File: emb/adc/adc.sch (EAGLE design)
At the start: 21 parts, among them IC1 AD623N, IC2 MCP3008, Q1 RD06HVF1, Q2 RD06HVF1, Q3 RD06HVF1, Q4 RD06HVF1

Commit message: new board
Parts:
- removed LED_YELLOW: (no value), adafruit:LED5MM
- removed Q4: RD06HVF1, transistor-power:RD06HVF1
- added R10, R9: 12K, rcl:R-US_0207/10
- IC1: value AD623N -> LM358N; device analog-devices:AD623N -> linear:LM358N
- Q1, Q2, Q3: value RD06HVF1 -> (none); device transistor-power:RD06HVF1 -> adafruit:MOSFET-NGDS_TO220V
- R1: value (none) -> 100K
- R2: value (none) -> 7.5K
- R3: value (none) -> 1.2K
- R4: value (none) -> 3.3K
- R5: value (none) -> 200
- R6, R7: value (none) -> 160
- R8: value (none) -> 12K
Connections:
- net N$12 renamed 3.3V
- removed net L_Y: J1.4, Q4.G
- removed net N$14: LED_RED.A, Q1.D
- removed net N$16: LED_GREEN.C, R6.1
- removed net N$17: LED_GREEN.A, Q2.D
- removed net N$18: LED_BLUE.C, R7.1
- removed net N$19: LED_YELLOW.C, R8.1
- removed net N$20: LED_BLUE.A, Q3.D
- removed net N$21: LED_YELLOW.A, Q4.D
- removed net VCC: IC2.GND
- new net 4.5V: IC1P.V+, R2.2, R3.2
- new net N$12: LED_GREEN.A, R6.1
- new net N$8: LED_BLUE.A, R7.1
- net 0V: now also D1.A, IC1A.-IN, IC1P.V-, IC2.GND, R10.1, R4.2, R8.2, R9.2; no longer IC1.-, IC1.REF, Q4.S, R3.2
- net 12V: now also R2.1; no longer D1.A, IC1.+V, R4.2, R8.2
- net L_B: now also R10.2
- net L_G: now also R9.1
- net L_R: now also R8.1
- net N$1: now also D1.C, IC1A.+IN; no longer IC1.RG@1
- net N$13: now also LED_GREEN.C, Q2.D; no longer LED_RED.C, R5.1
- net N$2: now also LED_BLUE.C, Q3.D; no longer IC1.RG@2, R1.1
- net N$3: now also LED_RED.A, R5.1; no longer D1.C, R2.1
- net N$6: now also LED_RED.C, Q1.D; no longer IC1.+, R2.2
- net N$7: now also IC1A.OUT, R1.1; no longer IC1.OUT
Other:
- note added: "1.9 - rød"
- note added: "3.2 - grøn og blå"
- note added: "forward voltage"
- note removed: "5V"
- moved on the sheet: D1, LED_BLUE, LED_GREEN, LED_RED, R1, R2, R3, R4, R7, R8

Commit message: adc files updated
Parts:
- added J3: (no value), con-amp:MTA02-100
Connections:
- new net N$99: D1.A, IC1A.+IN, J3.2
- net 0V: now also J3.1; no longer D1.A, IC1A.-IN
- net N$1: now also IC1A.-IN; no longer IC1A.+IN
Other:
- note added: "jumper between the two pins. Used to meassure current"
- moved on the sheet: IC1A
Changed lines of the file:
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@@
 <part name="4.5V" library="supply1" deviceset="VCC" device="" value="4.5V"/>
 <part name="3.3V2" library="supply1" deviceset="VCC" device="" value="3.3V"/>
+<part name="J3" library="con-amp" deviceset="MTA02-100" device=""/>
 </parts>
 <sheets>
@@
 <text x="170.18" y="83.82" size="1.778" layer="91">1.9 - rød</text>
 <text x="170.18" y="91.44" size="1.778" layer="91">forward voltage</text>
+<text x="22.86" y="43.18" size="1.778" layer="91">jumper between the two pins.
+Used to meassure current</text>
 </plain>
 <instances>
@@
 <instance part="P+32" gate="VCC" x="114.3" y="45.72" rot="R180"/>
 <instance part="P+33" gate="VCC" x="116.84" y="60.96" rot="R270"/>
-<instance part="IC1" gate="A" x="53.34" y="66.04"/>
+<instance part="IC1" gate="A" x="53.34" y="66.04" rot="MR180"/>
 <instance part="IC1" gate="P" x="53.34" y="66.04"/>
 <instance part="4.5V2" gate="VCC" x="53.34" y="78.74"/>
@@
 <instance part="4.5V" gate="VCC" x="121.92" y="106.68" rot="R270"/>
 <instance part="3.3V2" gate="VCC" x="121.92" y="66.04" rot="R270"/>
+<instance part="J3" gate="G$1" x="25.4" y="55.88" rot="R90"/>
 </instances>
 <busses>
@@
 <net name="N$7" class="0">
 <segment>
-<wire x1="60.96" y1="66.04" x2="66.04" y2="66.04" width="0.1524" layer="91"/>
 <pinref part="IC2" gate="G$1" pin="CH0"/>
-<pinref part="IC1" gate="A" pin="OUT"/>
 <pinref part="R1" gate="G$1" pin="1"/>
 <wire x1="66.04" y1="66.04" x2="81.28" y2="66.04" width="0.1524" layer="91"/>
 <wire x1="55.88" y1="83.82" x2="66.04" y2="83.82" width="0.1524" layer="91"/>
 <wire x1="66.04" y1="83.82" x2="66.04" y2="66.04" width="0.1524" layer="91"/>
+<pinref part="IC1" gate="A" pin="OUT"/>
+<wire x1="60.96" y1="66.04" x2="66.04" y2="66.04" width="0.1524" layer="91"/>
 </segment>
 </net>
@@
 <wire x1="114.3" y1="60.96" x2="109.22" y2="60.96" width="0.1524" layer="91"/>
 <pinref part="P+33" gate="VCC" pin="VCC"/>
-</segment>
-<segment>
-<pinref part="IC1" gate="P" pin="V-"/>
-<pinref part="P+2" gate="VCC" pin="VCC"/>
-<wire x1="53.34" y1="55.88" x2="53.34" y2="58.42" width="0.1524" layer="91"/>
-<wire x1="43.18" y1="60.96" x2="35.56" y2="60.96" width="0.1524" layer="91"/>
-<pinref part="D1" gate="1" pin="A"/>
-<wire x1="35.56" y1="60.96" x2="35.56" y2="63.5" width="0.1524" layer="91"/>
-<pinref part="IC1" gate="A" pin="-IN"/>
-<wire x1="45.72" y1="63.5" x2="43.18" y2="63.5" width="0.1524" layer="91"/>
-<wire x1="43.18" y1="63.5" x2="43.18" y2="60.96" width="0.1524" layer="91"/>
-<wire x1="35.56" y1="60.96" x2="35.56" y2="58.42" width="0.1524" layer="91"/>
-<wire x1="35.56" y1="58.42" x2="53.34" y2="58.42" width="0.1524" layer="91"/>
 </segment>
 <segment>
@@
 <pinref part="P+6" gate="VCC" pin="VCC"/>
 <wire x1="101.6" y1="91.44" x2="96.52" y2="91.44" width="0.1524" layer="91"/>
+</segment>
+<segment>
+<pinref part="IC1" gate="P" pin="V-"/>
+<pinref part="P+2" gate="VCC" pin="VCC"/>
+<pinref part="J3" gate="G$1" pin="1"/>
+<wire x1="27.94" y1="55.88" x2="53.34" y2="55.88" width="0.1524" layer="91"/>
+<wire x1="53.34" y1="55.88" x2="53.34" y2="58.42" width="0.1524" layer="91"/>
 </segment>
 </net>
@@
 <wire x1="35.56" y1="71.12" x2="35.56" y2="83.82" width="0.1524" layer="91"/>
 <wire x1="35.56" y1="83.82" x2="45.72" y2="83.82" width="0.1524" layer="91"/>
-<pinref part="IC1" gate="A" pin="+IN"/>
+<pinref part="IC1" gate="A" pin="-IN"/>
 <wire x1="45.72" y1="68.58" x2="43.18" y2="68.58" width="0.1524" layer="91"/>
 <wire x1="43.18" y1="68.58" x2="43.18" y2="71.12" width="0.1524" layer="91"/>
@@
 </segment>
 </net>
+<net name="N$99" class="0">
+<segment>
+<pinref part="D1" gate="1" pin="A"/>
+<wire x1="35.56" y1="63.5" x2="35.56" y2="60.96" width="0.1524" layer="91"/>
+<pinref part="J3" gate="G$1" pin="2"/>
+<wire x1="35.56" y1="60.96" x2="35.56" y2="58.42" width="0.1524" layer="91"/>
+<wire x1="27.94" y1="58.42" x2="35.56" y2="58.42" width="0.1524" layer="91"/>
+<pinref part="IC1" gate="A" pin="+IN"/>
+<wire x1="45.72" y1="63.5" x2="43.18" y2="63.5" width="0.1524" layer="91"/>
+<wire x1="43.18" y1="63.5" x2="43.18" y2="60.96" width="0.1524" layer="91"/>
+<wire x1="43.18" y1="60.96" x2="35.56" y2="60.96" width="0.1524" layer="91"/>
+</segment>
+</net>
 </nets>
 </sheet>
@@
 </schematic>
 </drawing>
+<compatibility>
+<note version="6.3" minversion="6.2.2" severity="warning">
+Since Version 6.2.2 text objects can contain more than one line,
+which will not be processed correctly with this version.
+</note>
+</compatibility>
 </eagle>

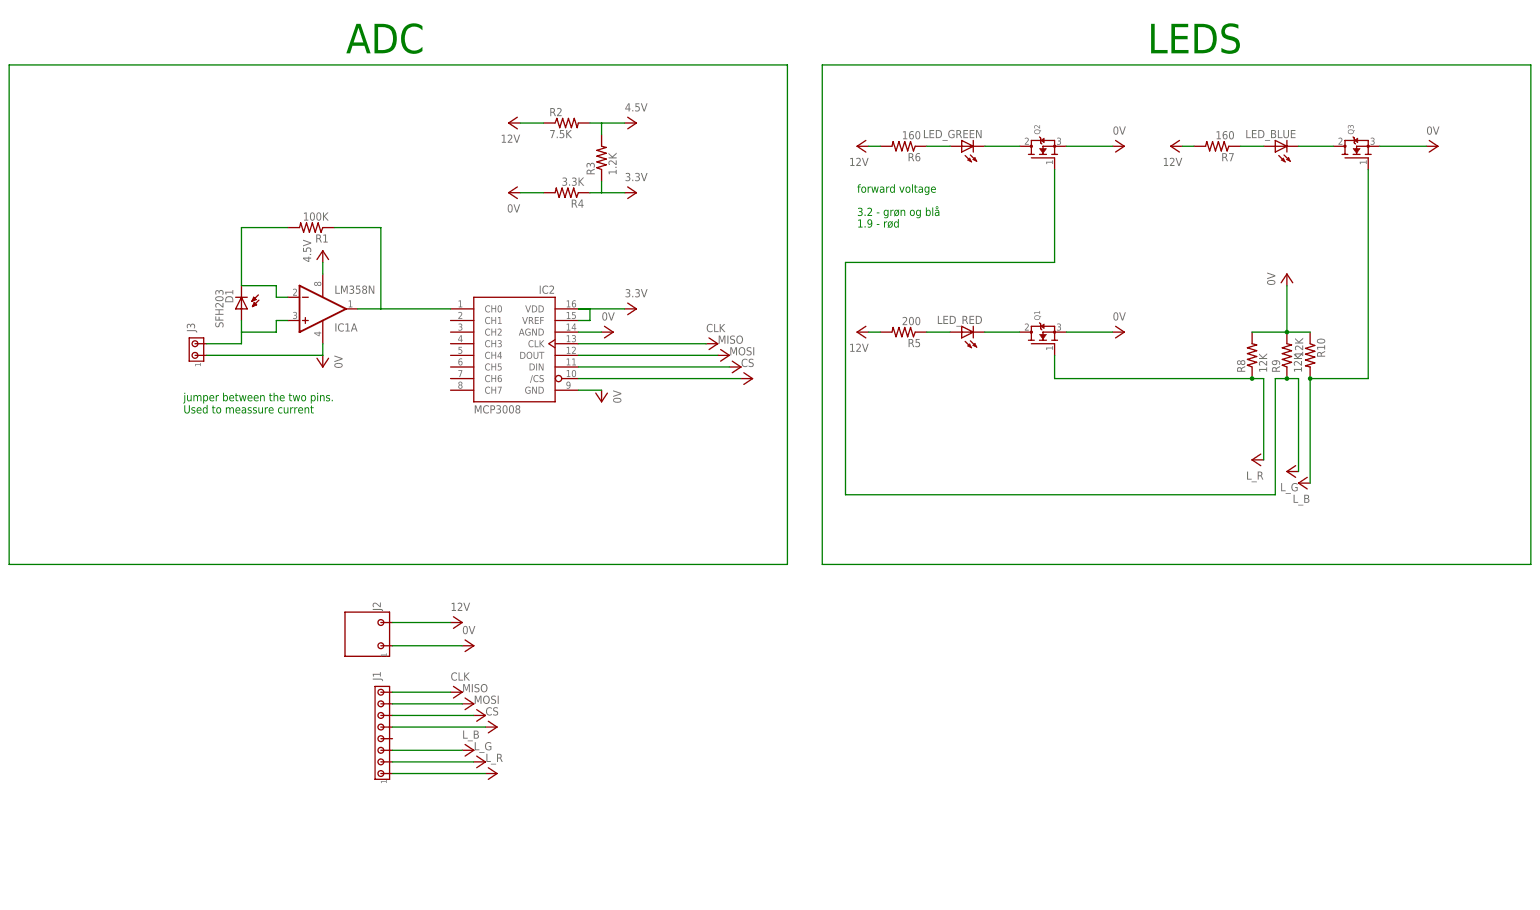
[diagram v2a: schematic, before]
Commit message: included figure of the adc board
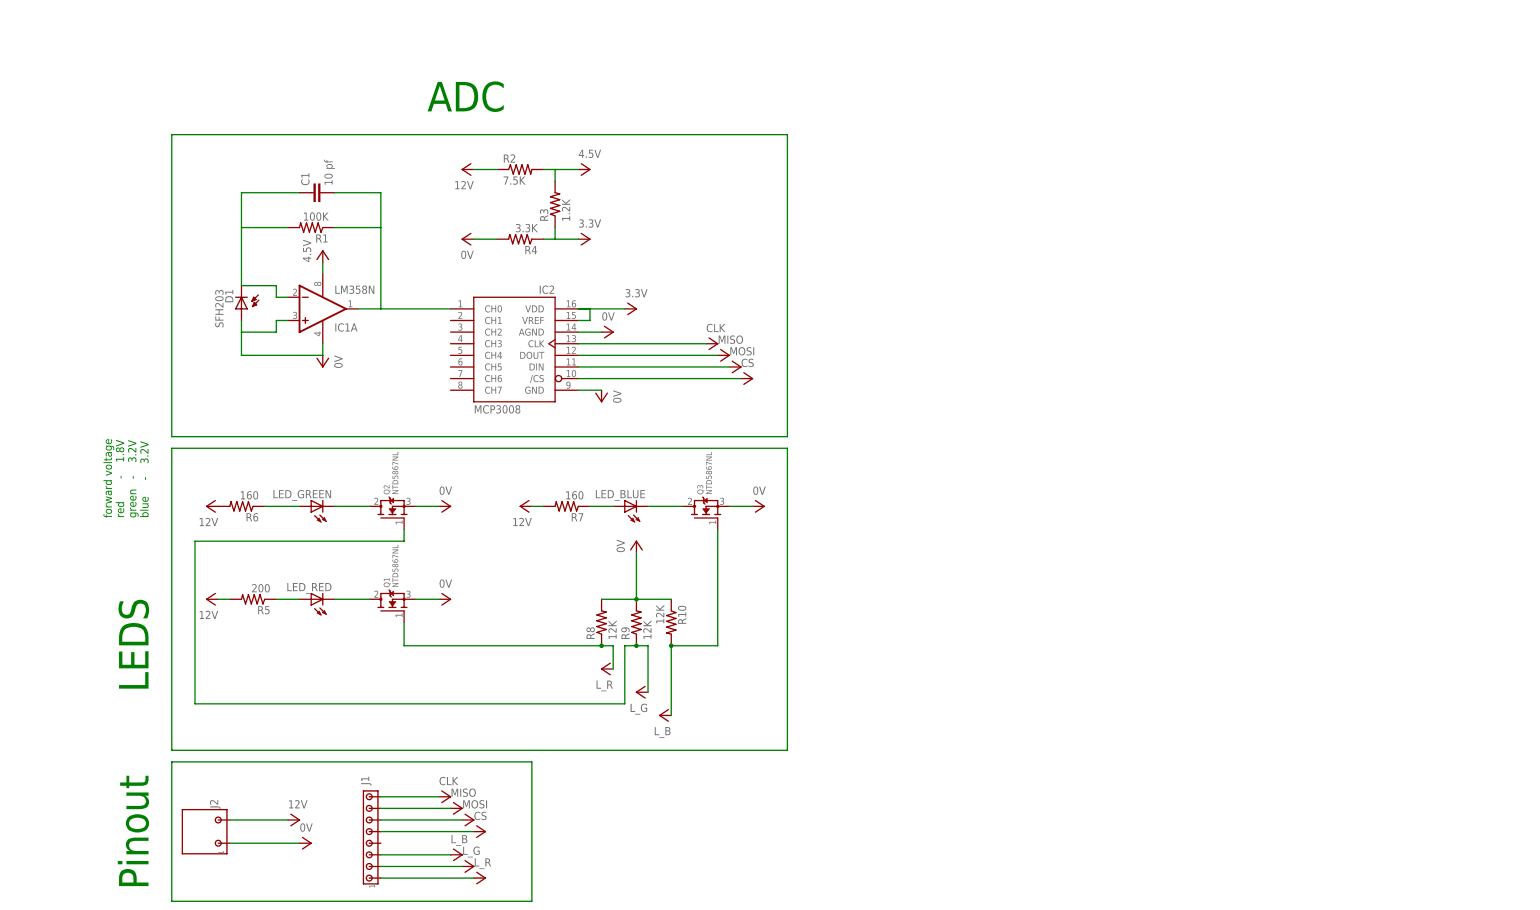
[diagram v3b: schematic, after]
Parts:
- removed J3: (no value), con-amp:MTA02-100
- added C1: 10 pf, capacitor-wima:C5/2.5
- Q1, Q2, Q3: value (none) -> NTD5867NL
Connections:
- removed net N$99: D1.A, IC1A.+IN, J3.2
- net 0V: now also D1.A, IC1A.+IN; no longer J3.1
- net N$1: now also C1.1
- net N$7: now also C1.2
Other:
- note added: "Pinout"
- note added: "forward voltage red - 1.8V green - 3.2V blue - 3.2V"
- note removed: "1.9 - rød"
- note removed: "3.2 - grøn og blå"
- note removed: "forward voltage"
- note removed: "jumper between the two pins. Used to meassure current"
- moved on the sheet: J1, J2, LED_BLUE, LED_GREEN, LED_RED, Q1, Q2, Q3, R10, R2, R3, R4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

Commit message: eagle files
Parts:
- IC1: value LM358N -> LM2904
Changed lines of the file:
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@@
 <part name="P+32" library="supply1" deviceset="VCC" device="" value="0V"/>
 <part name="P+33" library="supply1" deviceset="VCC" device="" value="0V"/>
-<part name="IC1" library="linear" deviceset="LM358" device="N"/>
+<part name="IC1" library="linear" deviceset="LM358" device="N" value="LM2904"/>
 <part name="4.5V2" library="supply1" deviceset="VCC" device="" value="4.5V"/>
 <part name="3.3V1" library="supply1" deviceset="VCC" device="" value="3.3V"/>
